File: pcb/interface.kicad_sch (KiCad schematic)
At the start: 46 parts, among them J17 BM04B-SRSS-TB, J18 BM04B-SRSS-TB, J4 BM03B-SRSS-TB, J9 BM08B-SRSS-TB

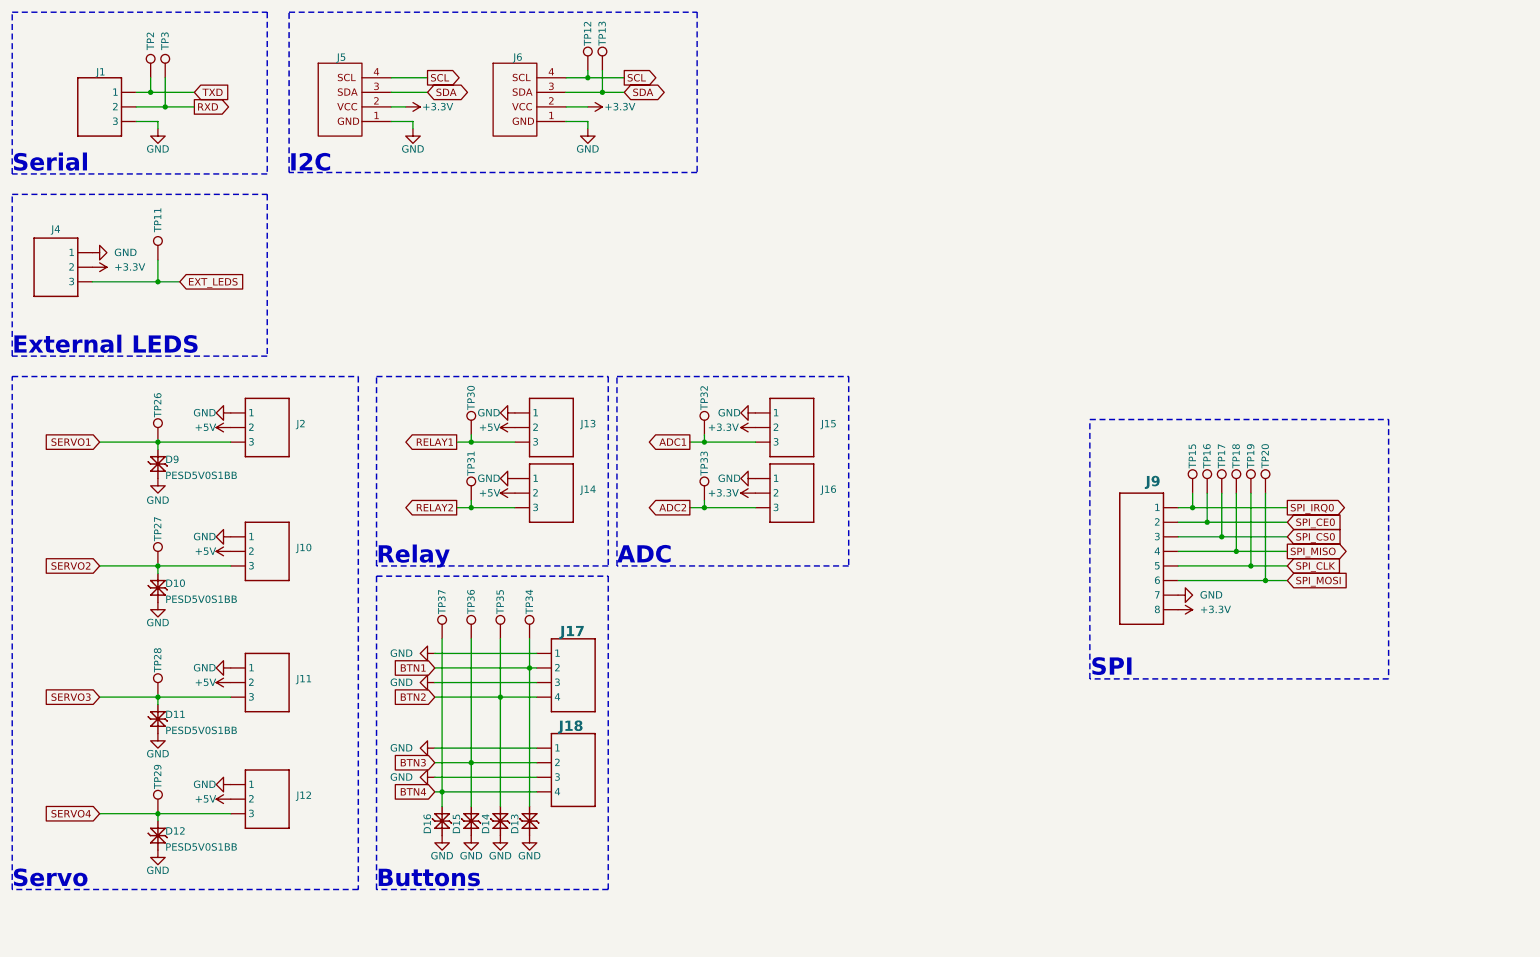
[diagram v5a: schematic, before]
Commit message: Added renders and aligned connectors
Added renders
Aligned connectors to grid
Added dimensions
Fixed part numbers and values
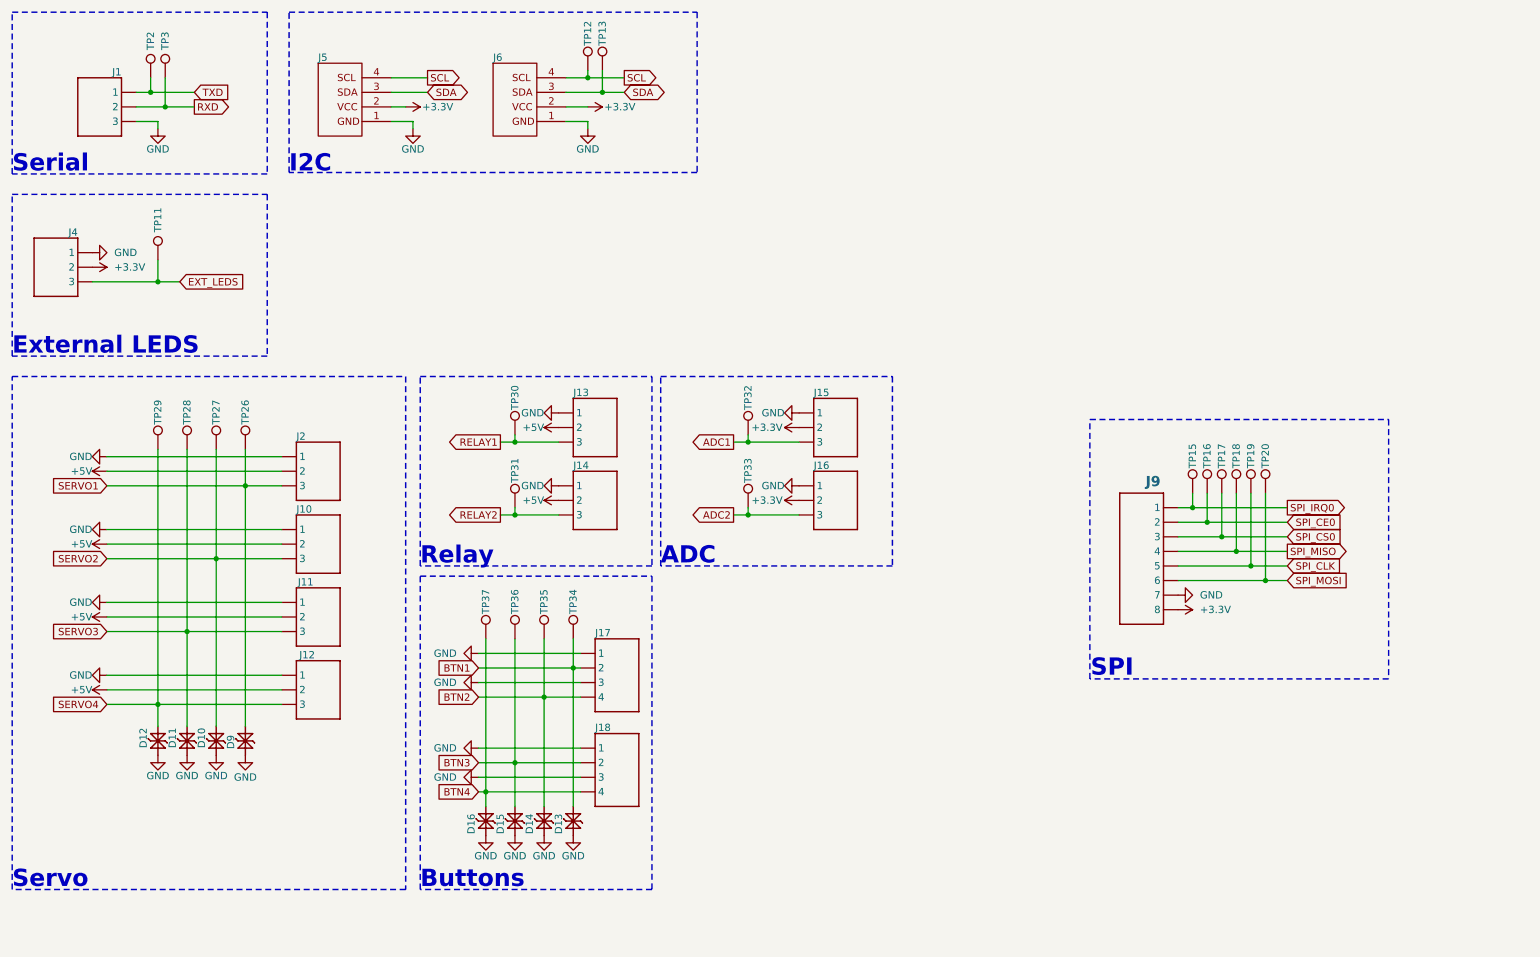
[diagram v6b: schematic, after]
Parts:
- J1: LCSC C2919600 -> C2919601; MPN BM03B-SRSS-TB -> BM04B-SRSS-TB; Mouser 306-BM03BSRSSTBLFSNP -> 306-BM04BSRSSTBTLFSN
- J10, J11, J12, J13, J14, J15, J16, J2: Digikey 455-BM03B-SRSS-TBTR-ND -> (none); LCSC C2919600 -> C2919601; MPN BM03B-SRSS-TB -> BM04B-SRSS-TB; Mouser 306-BM03BSRSSTBLFSNP -> 306-BM04BSRSSTBTLFSN
- J17, J18: value BM04B-SRSS-TB -> ~
- J4: value BM03B-SRSS-TB -> ~; Digikey 455-BM03B-SRSS-TBTR-ND -> (none); LCSC C2919600 -> C2919601; MPN BM03B-SRSS-TB -> BM04B-SRSS-TB; Mouser 306-3BSRSSTBTLP -> 306-BM04BSRSSTBTLFSN
- J9: value BM08B-SRSS-TB -> ~
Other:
- title: Client Hardware -> Client
- moved on the sheet: D10, D11, D12, D13, D14, D15, D16, D9, J10, J11, J12, J13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
